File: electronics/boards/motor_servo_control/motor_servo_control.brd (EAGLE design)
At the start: 48 x 48 mm, 46 parts, among them IC1 ATMEGA328P-MU, IC2 CP2104-F03-GMR, IC3 NCP1117ST50T3G, IC4 LMV358IDGKRG4, J1 GROVE_CONNECTOR2.0_1X4, J2 GROVE_CONNECTOR2.0_1X4, J3 10129383-906001ALF, J4 10129383-912001ALF, J5 10129383-912001ALF, Q1 FDN340P, X1 MINI-USB-SHIELD-UX60A-MB-5ST, Y1 X322516MLB4SI

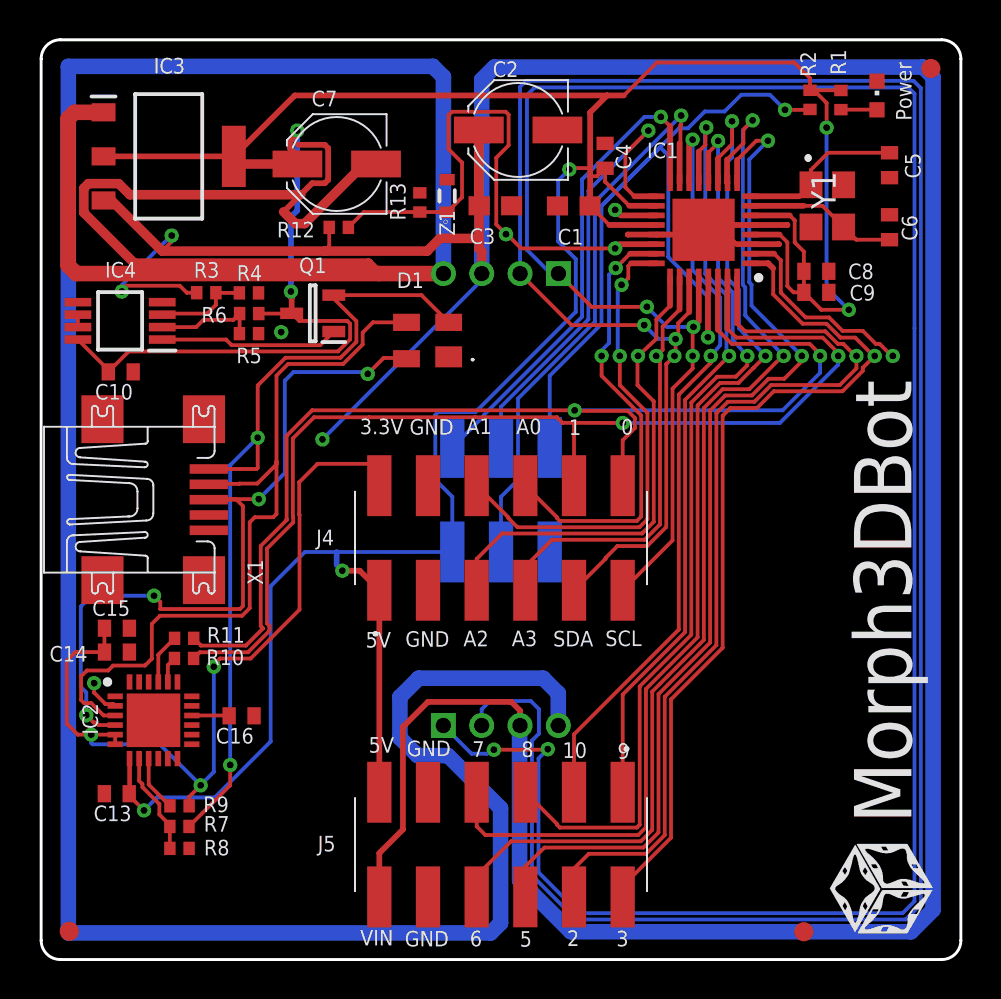
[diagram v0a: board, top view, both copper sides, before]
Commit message: - mega328 Platine layout angepasst zum handlöten - Motorplatine eingefügt (2 DC oder 1 Stepper + 8 Servos)
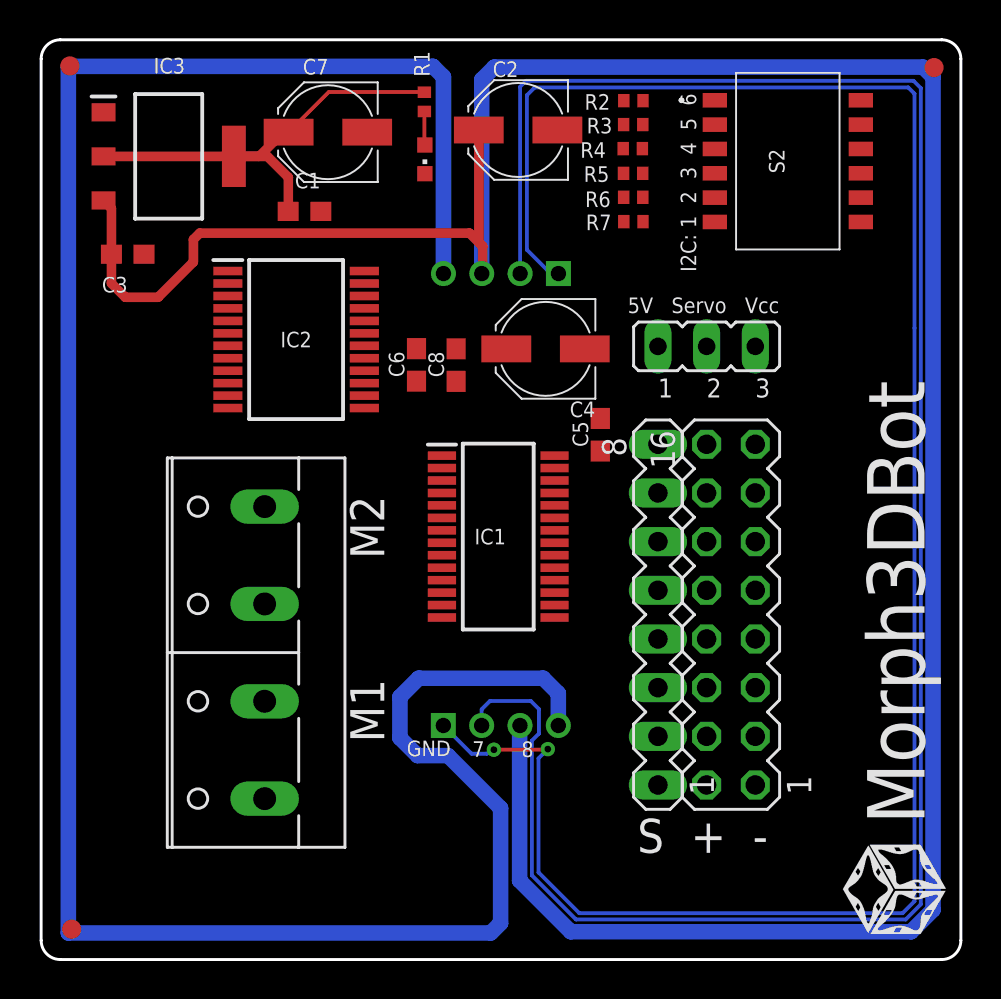
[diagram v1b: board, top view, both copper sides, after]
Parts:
- removed C10, C14, C9: CL05B104KO5NNNC - 100n, rcl:C0402
- removed C13, C15: CL05A105KA5NQNC - 1uF, rcl:C0402
- removed C16: CL05A475MP5NRNC - 4.7uF, rcl:C0402
- removed D1: SP0503BAHTG, samacsys:SP0503BAHTG
- removed IC4: LMV358IDGKRG4, samacsys:SOP65P490X110-8N
- removed J3: 10129383-906001ALF, samacsys:10129383906001ALF
- removed J4, J5: 10129383-912001ALF, samacsys:10129383912001ALF
- removed Q1: FDN340P, samacsys:SOT95P237X112-3N
- removed R10, R11, R12: Uniroyal Elec 0402WGF1001TCE - 1k, rcl:R0402
- removed R13: Uniroyal Elec 0402WGF6801TCE - 680R, rcl:R0402
- removed R8: Uniroyal Elec 0402WGF4702TCE - 47k, rcl:R0402
- removed R9: Uniroyal Elec 0402WGF4701TCE - 4k7, rcl:R0402
- removed Y1: X322516MLB4SI, samacsys:X322516MLB4SI
- removed Z1: EDZTE615.1B, samacsys:EMD2
- added JP1: (no value), jumper:JP2
- added S2: DSHP06TSGET, samacsys:DSHP06TSGET
- added SV1: (no value), con-lstb:MA08-2
- added SV2: (no value), con-lstb:MA08-1
- C4: value CL05B104KO5NNNC - 100n -> ST(Semtech) CK1C470M-CRD54 - 47uF; device rcl:C0402 -> rcl:PANASONIC_C
- C5, C6: value 0402CG150J500NT - 15pF -> Walsin Tech Corp 0603B104K250CT - 100nF; device rcl:C0402 -> rcl:C0603
- C8: value CL05B104KO5NNNC - 100n -> CL10A105KB8NNNC - 1uF; device rcl:C0402 -> rcl:C0603
- IC1: value ATMEGA328P-MU -> PCA9685PW; device samacsys:QFN50P500X500X100-33N -> samacsys:SOP65P640X110-28N
- IC2: value CP2104-F03-GMR -> TB6612FNG,C,8,EL; device samacsys:QFN50P400X400X80-25N -> samacsys:SOP65P760X160-24N
- R2: value Uniroyal Elec 0402WGF1002TCE - 10kR -> 0402WGF1002TCE - 10k
- R3, R4: value Uniroyal Elec 0402WGF1002TCE - 10k -> 0402WGF1002TCE - 10k
- R5: value Uniroyal Elec 0402WGF1001TCE - 1k -> 0402WGF1002TCE - 10k
- R6: value Uniroyal Elec 0402WGF1801TCE - 1k8 -> 0402WGF1002TCE - 10k
- R7: value Uniroyal Elec 0402WGF2402TCE - 24k -> 0402WGF1002TCE - 10k
- X1: value MINI-USB-SHIELD-UX60A-MB-5ST -> (none); device con-hirose:UX60A-MB-5ST -> con-wago-508:W237-4P
- moved FID2 59.2 mm to (1.50, 46.6)
- moved R7 39.5 mm to (30.9, 38.5), turned to 180 degrees
- moved C6 25.7 mm to (19.6, 31.0), turned to 90 degrees
- moved R3 23.9 mm to (30.9, 43.6), turned to 180 degrees
- moved LED1 23.8 mm to (20.0, 41.8), turned to 180 degrees
- moved R1 21.7 mm to (20.0, 44.8)
- moved R4 21.4 mm to (30.9, 42.3), turned to 180 degrees
- moved R5 21.3 mm to (30.9, 41.0)
- moved R6 21.3 mm to (30.9, 39.8), turned to 180 degrees
- moved IC2 21.2 mm to (13.3, 32.4)
- moved C5 20.6 mm to (29.2, 27.4)
- moved C8 19.4 mm to (21.7, 31.0), turned to 90 degrees
- moved C3 19.4 mm to (4.52, 36.8)
- moved IC1 19.3 mm to (23.9, 22.1), turned to 0 degrees
- moved C1 14.1 mm to (13.7, 39.0), turned to 0 degrees
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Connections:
- removed net +3V3: C14.2, C15.2, IC2.5, IC2.6, J4.B1, R9.2
- removed net ADC6: IC1.19
- removed net ADC7: IC1.22, R12.1, R13.2, Z1.1
- removed net GATE_CMD: IC4.1, Q1.1
- removed net MISO: IC1.16, J3.A1
- removed net MOSI: IC1.15, J3.B2
- removed net N$3: C6.2, IC1.7, Y1.3
- removed net N$4: IC4.6, IC4.7
- removed net N$5: IC2.8, R7.1, R8.1
- removed net N$6: IC2.9, R9.1
- removed net N$7: C16.2, IC2.16
- removed net N$8: IC2.21, R11.1
- removed net N$9: IC2.20, R10.1
- removed net OPAMP-NEG: IC4.2, R5.2, R6.1
- removed net OPAMP-POS: IC4.3, R3.2, R4.1
- removed net PB0: IC1.12, J5.A3
- removed net PB1: IC1.13, J5.A1
- removed net PB2: IC1.14, J5.A2
- removed net PC0: IC1.23, J4.B4
- removed net PC1: IC1.24, J4.B3
- removed net PC2: IC1.25, J4.A3
- removed net PC3: IC1.26, J4.A4
- removed net PC4/SDA: IC1.27, J1.2, J2.2, J4.A5
- removed net PC5/SCL: IC1.28, J1.1, J2.1, J4.A6
- removed net PD2: IC1.32, J5.B2
- removed net PD3: IC1.1, J5.B1
- removed net PD4: IC1.2
- removed net PD5: IC1.9, J5.B3
- removed net PD6: IC1.10, J5.B4
- removed net PD7: IC1.11, J5.A4
- removed net RESET: IC1.29, J3.A3, R2.1
- removed net SCK: IC1.17, J3.A2
- removed net UART_MEGA_RXD: IC1.30, J4.B6, R11.2
- removed net UART_MEGA_TXD: IC1.31, J4.B5, R10.2
- removed net USBVCC: D1.2, Q1.2, R7.2, X1.1
- removed net USB_DN: D1.4, IC2.4, X1.3
- removed net USB_DP: D1.3, IC2.3, X1.2
- new net A0: IC1.1, R7.1, S2.6
- new net A1: IC1.2, R6.1, S2.5
- new net A2: IC1.3, R5.1, S2.4
- new net A3: IC1.4, R4.1, S2.3
- new net A4: IC1.5, R3.1, S2.2
- new net A5: IC1.24, R2.1, S2.1
- new net M1+: IC2.1, IC2.2, X1.1
- new net M1-: IC2.5, IC2.6, X1.2
- new net M2+: IC2.7, IC2.8, X1.3
- new net M2-: IC2.11, IC2.12, X1.4
- new net PWM0: IC1.6
- new net PWM1: IC1.7
- new net PWM10: IC1.17, SV2.3
- new net PWM11: IC1.18, SV2.4
- new net PWM12: IC1.19, SV2.5
- new net PWM13: IC1.20, SV2.6
- new net PWM14: IC1.21, SV2.7
- new net PWM15: IC1.22, SV2.8
- new net PWM2: IC1.8, IC2.23
- new net PWM3: IC1.9, IC2.22
- new net PWM4: IC1.10, IC2.21
- new net PWM5: IC1.11, IC2.17
- new net PWM6: IC1.12, IC2.16
- new net PWM7: IC1.13, IC2.15
- new net PWM8: IC1.15, SV2.1
- new net PWM9: IC1.16, SV2.2
- new net SCL: IC1.26, J1.1, J2.1
- new net SDA: IC1.27, J1.2, J2.2
- net +5V: now also C5.1, C6.1, C8.1, IC1.28, IC2.19, IC2.20, JP1.1, S2.10, S2.11, S2.12, S2.7, S2.8, S2.9; no longer C10.2, C13.2, C4.1, C8.2, C9.2, IC1.18, IC1.20, IC1.4, IC1.6, IC2.7, IC4.8, J3.B1, J4.A1, J5.A6, Q1.3, R2.2, R5.1
- net GND: now also C4.-, C5.2, C6.2, C8.2, IC1.14, IC1.23, IC1.25, IC2.10, IC2.18, IC2.3, IC2.4, IC2.9, R2.2, R3.2, R5.2, R7.2, SV1.1, SV1.11, SV1.13, SV1.15, SV1.3, SV1.5, SV1.7, SV1.9; no longer C10.1, C13.1, C14.1, C15.1, C16.1, C4.2, C5.1, C6.1, C8.1, C9.1, D1.1, IC1.21, IC1.3, IC1.33, IC1.5, IC2.2, IC4.4, IC4.5, J3.B3, J4.A2, J4.B2, J5.A5, J5.B5, R13.1, R8.2, X1.5, Y1.2, Y1.4, Z1.2
- net N$2: now also JP1.2, SV1.10, SV1.12, SV1.14, SV1.16, SV1.2, SV1.4, SV1.6, SV1.8; no longer C5.2, IC1.8, Y1.1
- net VCC: now also C4.+, IC2.13, IC2.14, IC2.24, JP1.3; no longer J5.B6, R12.2, R3.1
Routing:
- net +5V: track 191.4 -> 23.9 mm, vias 7 -> 0
- net PC4/SDA: track 137.4 -> 0.00 mm, vias 3 -> 0
- net PC5/SCL: track 132.6 -> 0.00 mm, vias 5 -> 0
- net SDA: track 0.00 -> 108.1 mm
- net SCL: track 0.00 -> 106.4 mm, vias 0 -> 2
- net GND: track 212.4 -> 124.3 mm, vias 2 -> 0
- net UART_MEGA_RXD: track 60.7 -> 0.00 mm, vias 2 -> 0
- net UART_MEGA_TXD: track 58.5 -> 0.00 mm, vias 2 -> 0
- net PD6: track 56.9 -> 0.00 mm, vias 2 -> 0
- net PD7: track 55.4 -> 0.00 mm, vias 2 -> 0
- net PD5: track 54.5 -> 0.00 mm, vias 2 -> 0
- net PB0: track 48.4 -> 0.00 mm, vias 2 -> 0
- net PD2: track 48.4 -> 0.00 mm, vias 1 -> 0
- net PD3: track 45.9 -> 0.00 mm, vias 1 -> 0
- net RESET: track 45.8 -> 0.00 mm, vias 2 -> 0
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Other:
- board text added: "5V Servo Vcc"
- board text added: "I2C: 1 2 3 4 5 6"
- board text added: "M1 M2"
- board text added: "S + -"
- board text removed: "0"
- board text removed: "1"
- board text removed: "10"
- board text removed: "2"
- board text removed: "3"
- board text removed: "3.3V"
- board text removed: "5"
- board text removed: "5V"
- board text removed: "6"
- board text removed: "9"
- board text removed: "A0"
- board text removed: "A1"
- board text removed: "A2"
- board text removed: "A3"
- board text removed: "Power"
- board text removed: "SCL"
- board text removed: "SDA"
- board text removed: "VIN"

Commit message: ESP32-Template: - USB-Datenleitungen getauscht (BugFix) 328P-Template: - USB-Datenleitungen getauscht (BugFix) - Reset-Leitung mit DTR verbunden (Zum Programieren über ARDUINO-IDE notwendig)
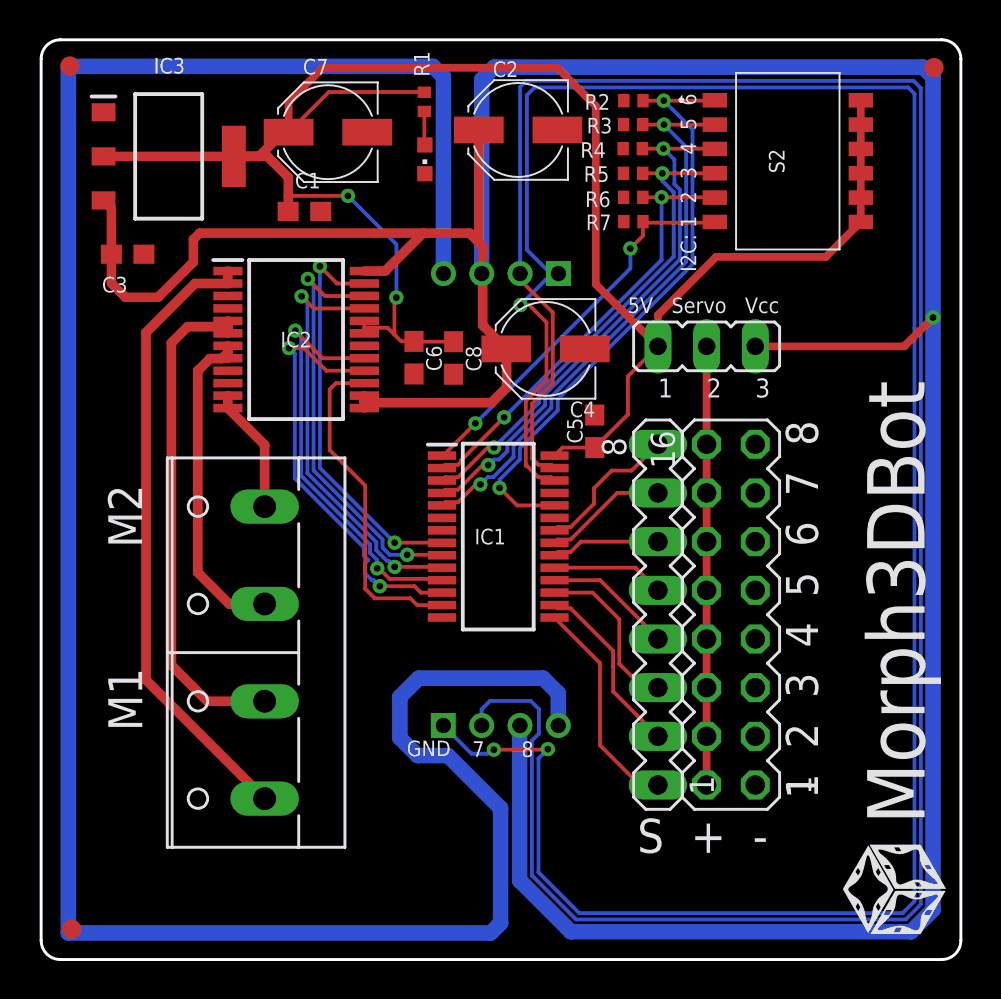
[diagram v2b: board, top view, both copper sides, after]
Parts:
- moved C6 0.40 mm to (19.5, 31.4), turned to 270 degrees
- moved C8 0.39 mm to (21.5, 31.4), turned to 270 degrees
- moved C5 0.34 mm to (28.9, 27.6)
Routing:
- net +5V: track 23.9 -> 103.5 mm, vias 0 -> 2
- net M1+: track 0.00 -> 32.9 mm
- net A5: track 0.00 -> 32.0 mm, vias 0 -> 2
- net A4: track 0.00 -> 30.1 mm, vias 0 -> 2
- net VCC: track 143.0 -> 171.7 mm, vias 0 -> 1
- net A3: track 0.00 -> 28.0 mm, vias 0 -> 2
- net M1-: track 0.00 -> 26.4 mm
- net A2: track 0.00 -> 25.6 mm, vias 0 -> 2
- net A1: track 0.00 -> 23.0 mm, vias 0 -> 2
- net N$2: track 0.00 -> 22.9 mm
- net PWM6: track 0.00 -> 22.4 mm, vias 0 -> 2
- net PWM3: track 0.00 -> 22.2 mm, vias 0 -> 2
- net PWM4: track 0.00 -> 22.2 mm, vias 0 -> 2
- net PWM5: track 0.00 -> 22.0 mm, vias 0 -> 2
- net PWM2: track 0.00 -> 21.2 mm, vias 0 -> 2
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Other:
- board text added: "1 2 3 4 5 6 7 8"

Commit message: Logo geändert
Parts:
- IC3: device samacsys:SOT230P700X180-4N@1 -> samacsys:SOT230P700X180-4N
